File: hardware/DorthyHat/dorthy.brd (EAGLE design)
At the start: 100 x 100 mm, 28 parts, among them J1 90325-0004, J2 90325-0004, U1 DEV-15583, U2 SN74AHC125N

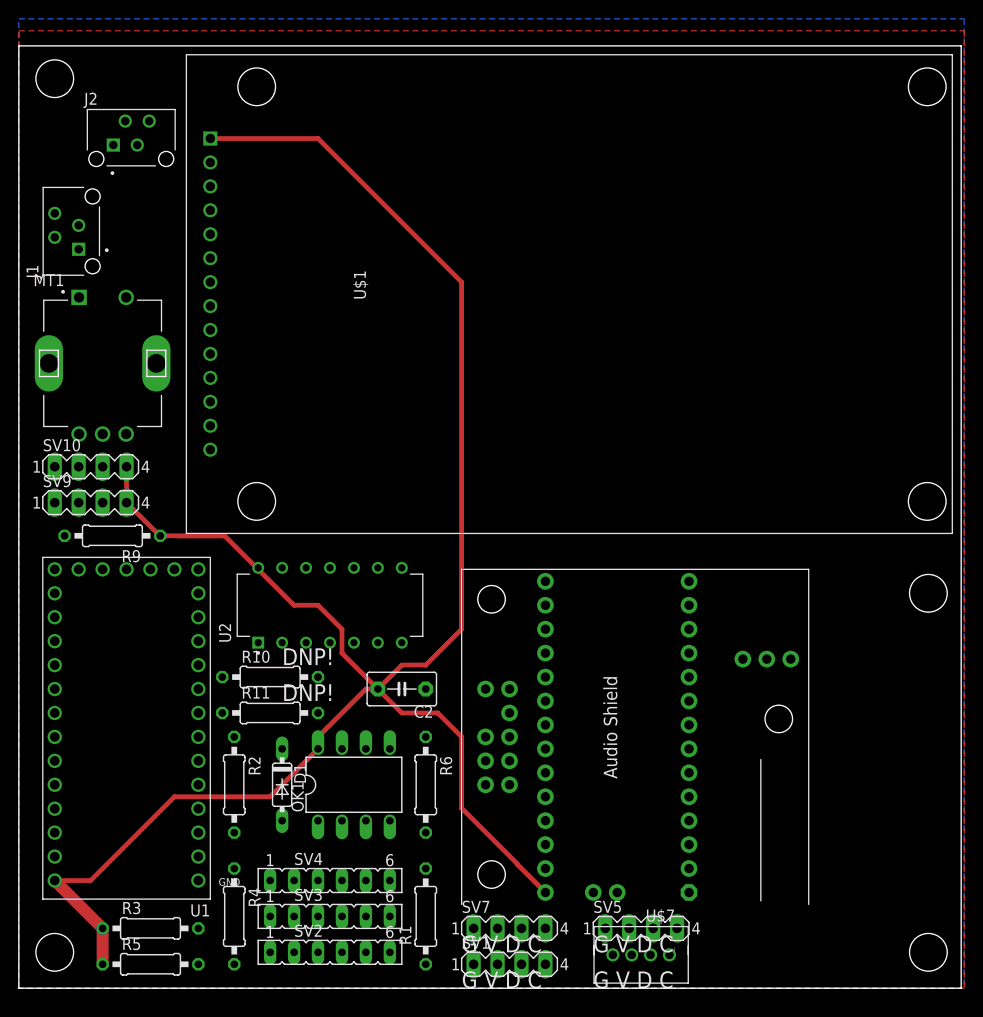
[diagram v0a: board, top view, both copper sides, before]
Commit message: change triangle to square wave, volume to 1.0 on output
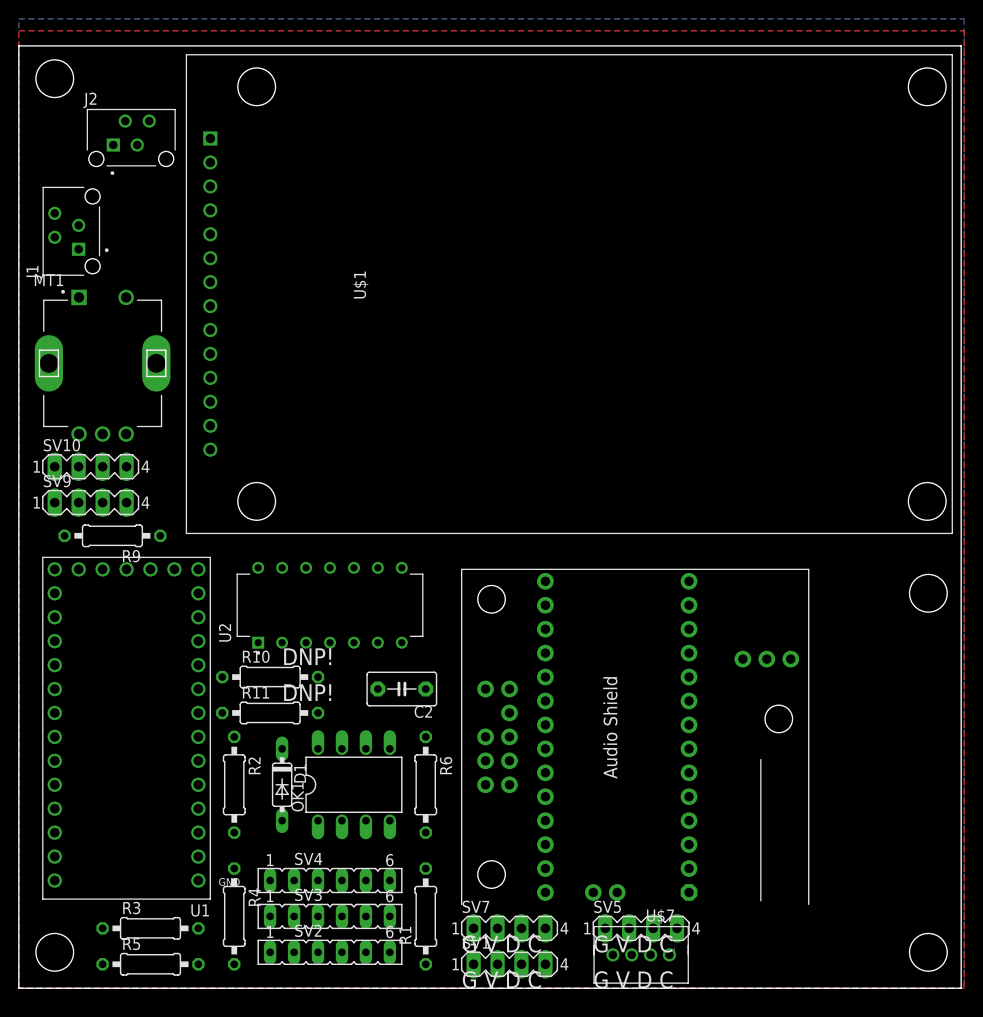
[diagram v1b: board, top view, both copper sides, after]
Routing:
- net VCC: track 207.2 -> 0.00 mm
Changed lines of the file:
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@@
 <setting verticaltext="up"/>
 </settings>
-<grid distance="0.5" unitdist="mm" unit="mm" style="lines" multiple="1" display="yes" altdistance="50" altunitdist="mil" altunit="mil"/>
+<grid distance="10" unitdist="mil" unit="mil" style="lines" multiple="1" display="yes" altdistance="10" altunitdist="mil" altunit="mil"/>
 <layers>
 <layer number="1" name="Top" color="4" fill="1" visible="yes" active="yes"/>
@@
 </class>
 </classes>
-<designrules name="default">
+<designrules name="default *">
 <description language="de">&lt;b&gt;EAGLE Design Rules&lt;/b&gt;
 &lt;p&gt;
@@
 <param name="mtCopper" value="0.035mm 0.035mm 0.035mm 0.035mm 0.035mm 0.035mm 0.035mm 0.035mm 0.035mm 0.035mm 0.035mm 0.035mm 0.035mm 0.035mm 0.035mm 0.035mm"/>
 <param name="mtIsolate" value="1.5mm 0.15mm 0.2mm 0.15mm 0.2mm 0.15mm 0.2mm 0.15mm 0.2mm 0.15mm 0.2mm 0.15mm 0.2mm 0.15mm 0.2mm"/>
-<param name="mdWireWire" value="6mil"/>
-<param name="mdWirePad" value="6mil"/>
-<param name="mdWireVia" value="6mil"/>
-<param name="mdPadPad" value="6mil"/>
-<param name="mdPadVia" value="6mil"/>
-<param name="mdViaVia" value="6mil"/>
+<param name="mdWireWire" value="10mil"/>
+<param name="mdWirePad" value="10mil"/>
+<param name="mdWireVia" value="10mil"/>
+<param name="mdPadPad" value="10mil"/>
+<param name="mdPadVia" value="10mil"/>
+<param name="mdViaVia" value="10mil"/>
 <param name="mdSmdPad" value="6mil"/>
 <param name="mdSmdVia" value="6mil"/>
@@
 <param name="mdDrill" value="6mil"/>
 <param name="mdSmdStop" value="0mil"/>
-<param name="msWidth" value="6mil"/>
+<param name="msWidth" value="10mil"/>
 <param name="msDrill" value="0.35mm"/>
 <param name="msMicroVia" value="9.99mm"/>
@@
 <param name="RoutingGrid" value="50mil"/>
 <param name="AutoGrid" value="1"/>
-<param name="Efforts" value="0"/>
+<param name="Efforts" value="2"/>
 <param name="TopRouterVariant" value="1"/>
 <param name="tpViaShape" value="round"/>
@@
 <vertex x="100.33" y="0"/>
 </polygon>
+<wire x1="62.23" y1="6.35" x2="55.88" y2="12.7" width="0" layer="19" extent="1-1"/>
+<wire x1="11.43" y1="44.45" x2="6.35" y2="51.53" width="0" layer="19" extent="1-1"/>
+<wire x1="48.26" y1="6.35" x2="55.88" y2="12.7" width="0" layer="19" extent="1-1"/>
+<wire x1="19.05" y1="11.43" x2="3.81" y2="13.97" width="0" layer="19" extent="1-1"/>
+<wire x1="25.4" y1="36.67" x2="11.43" y2="44.45" width="0" layer="19" extent="1-1"/>
+<wire x1="33.02" y1="36.67" x2="25.4" y2="36.67" width="0" layer="19" extent="1-1"/>
+<wire x1="40.64" y1="36.67" x2="33.02" y2="36.67" width="0" layer="19" extent="1-1"/>
+<wire x1="39.37" y1="25.4" x2="43.18" y2="31.75" width="0" layer="19" extent="1-1"/>
+<wire x1="27.94" y1="44.61" x2="25.4" y2="36.67" width="0" layer="19" extent="1-1"/>
 </signal>
 <signal name="VCC">
@@
 <contactref element="U$1" pad="VCC"/>
 <contactref element="U2" pad="14"/>
-<wire x1="3.81" y1="11.43" x2="8.89" y2="6.35" width="1.27" layer="1"/>
-<wire x1="8.89" y1="6.35" x2="8.89" y2="2.54" width="1.27" layer="1"/>
-<wire x1="26.67" y1="20.32" x2="31.75" y2="25.4" width="0.508" layer="1"/>
-<wire x1="26.67" y1="20.32" x2="16.51" y2="20.32" width="0.508" layer="1"/>
-<wire x1="31.75" y1="25.4" x2="31.75" y2="26.67" width="0.508" layer="1"/>
-<wire x1="36.83" y1="31.75" x2="38.1" y2="31.75" width="0.508" layer="1"/>
-<wire x1="31.75" y1="26.67" x2="36.83" y2="31.75" width="0.508" layer="1"/>
-<wire x1="38.1" y1="31.75" x2="40.64" y2="29.21" width="0.508" layer="1"/>
-<wire x1="40.64" y1="29.21" x2="44.45" y2="29.21" width="0.508" layer="1"/>
-<wire x1="44.45" y1="29.21" x2="46.99" y2="26.67" width="0.508" layer="1"/>
-<wire x1="52.8955" y1="13.1960125" x2="52.8955" y2="13.1445" width="0.508" layer="1"/>
-<wire x1="52.8955" y1="13.1445" x2="55.88" y2="10.16" width="0.508" layer="1"/>
-<wire x1="46.99" y1="19.1015125" x2="52.8955" y2="13.1960125" width="0.508" layer="1"/>
-<wire x1="46.99" y1="26.67" x2="46.99" y2="19.1015125" width="0.508" layer="1"/>
-<wire x1="38.1" y1="31.75" x2="34.29" y2="35.56" width="0.508" layer="1"/>
-<wire x1="34.29" y1="35.56" x2="34.29" y2="38.1" width="0.508" layer="1"/>
-<wire x1="34.29" y1="38.1" x2="31.75" y2="40.64" width="0.508" layer="1"/>
-<wire x1="31.75" y1="40.64" x2="29.21" y2="40.64" width="0.508" layer="1"/>
-<wire x1="29.21" y1="40.64" x2="25.4" y2="44.45" width="0.508" layer="1"/>
-<wire x1="25.4" y1="44.45" x2="25.4" y2="44.61" width="0.508" layer="1"/>
-<wire x1="25.4" y1="44.61" x2="25.24" y2="44.61" width="0.508" layer="1"/>
-<wire x1="25.24" y1="44.61" x2="21.86158125" y2="47.98841875" width="0.508" layer="1"/>
-<wire x1="21.86158125" y1="47.98841875" x2="15.01" y2="48.01" width="0.508" layer="1"/>
-<wire x1="15.01" y1="48.01" x2="14.95214375" y2="48.00785625" width="0.508" layer="1"/>
-<wire x1="14.95214375" y1="48.00785625" x2="11.43" y2="51.53" width="0.508" layer="1"/>
-<wire x1="11.43" y1="51.53" x2="11.43" y2="55.34" width="0.508" layer="1"/>
-<wire x1="38.1" y1="31.75" x2="40.64" y2="34.29" width="0.508" layer="1"/>
-<wire x1="40.64" y1="34.29" x2="43.18" y2="34.29" width="0.508" layer="1"/>
-<wire x1="43.18" y1="34.29" x2="46.99" y2="38.1" width="0.508" layer="1"/>
-<wire x1="46.99" y1="74.93" x2="31.75" y2="90.17" width="0.508" layer="1"/>
-<wire x1="31.75" y1="90.17" x2="20.32" y2="90.17" width="0.508" layer="1"/>
-<wire x1="46.99" y1="38.1" x2="46.99" y2="74.93" width="0.508" layer="1"/>
-<wire x1="7.62" y1="11.43" x2="3.81" y2="11.43" width="0.508" layer="1"/>
-<wire x1="16.51" y1="20.32" x2="7.62" y2="11.43" width="0.508" layer="1"/>
+<wire x1="11.43" y1="55.34" x2="20.32" y2="90.17" width="0" layer="19" extent="1-1"/>
+<wire x1="11.43" y1="51.53" x2="11.43" y2="55.34" width="0" layer="19" extent="1-1"/>
+<wire x1="15.01" y1="48.01" x2="11.43" y2="51.53" width="0" layer="19" extent="1-1"/>
+<wire x1="25.4" y1="44.61" x2="15.01" y2="48.01" width="0" layer="19" extent="1-1"/>
+<wire x1="38.1" y1="31.75" x2="25.4" y2="44.61" width="0" layer="19" extent="1-1"/>
+<wire x1="31.75" y1="25.4" x2="38.1" y2="31.75" width="0" layer="19" extent="1-1"/>
+<wire x1="55.88" y1="10.16" x2="38.1" y2="31.75" width="0" layer="19" extent="1-1"/>
+<wire x1="8.89" y1="6.35" x2="31.75" y2="25.4" width="0" layer="19" extent="1-1"/>
+<wire x1="8.89" y1="2.54" x2="8.89" y2="6.35" width="0" layer="19" extent="1-1"/>
+<wire x1="3.81" y1="11.43" x2="8.89" y2="6.35" width="0" layer="19" extent="1-1"/>
 </signal>
 <signal name="INMIDI4">
@@
 <vertex x="100.33" y="0"/>
 </polygon>
+<wire x1="10.025" y1="89.48" x2="6.35" y2="78.415" width="0" layer="19" extent="1-1"/>
+<wire x1="20.32" y1="82.55" x2="10.025" y2="89.48" width="0" layer="19" extent="1-1"/>
+<wire x1="50.8" y1="6.35" x2="55.88" y2="15.24" width="0" layer="19" extent="1-1"/>
+<wire x1="64.77" y1="6.35" x2="55.88" y2="15.24" width="0" layer="19" extent="1-1"/>
+<wire x1="65.04" y1="3.54" x2="64.77" y2="6.35" width="0" layer="19" extent="1-1"/>
+<wire x1="22.86" y1="16.51" x2="3.81" y2="16.51" width="0" layer="19" extent="1-1"/>
+<wire x1="21.59" y1="29.21" x2="22.86" y2="16.51" width="0" layer="19" extent="1-1"/>
+<wire x1="21.59" y1="33.02" x2="21.59" y2="29.21" width="0" layer="19" extent="1-1"/>
+<wire x1="13.97" y1="44.45" x2="21.59" y2="33.02" width="0" layer="19" extent="1-1"/>
+<wire x1="8.89" y1="51.53" x2="13.97" y2="44.45" width="0" layer="19" extent="1-1"/>
 </signal>
 <signal name="RXBUF">
